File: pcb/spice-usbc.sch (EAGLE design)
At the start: 39 parts, among them J1 USB-C, J2 2X8, U1 MCP1700T-3302TT, U10 74LVC1G17, U11 74HC541, U12 74LVC1G17, U13 74LVC1G17, U14 74LVC1G17, U15 74LVC1G17, U16 74LVC1G17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

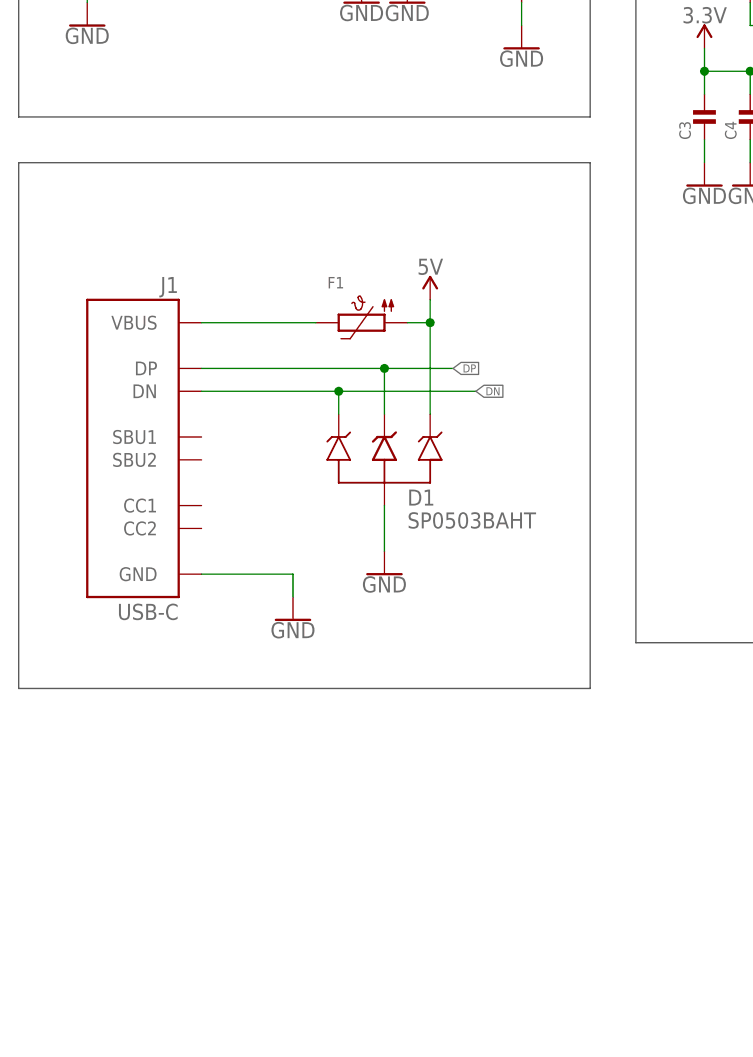
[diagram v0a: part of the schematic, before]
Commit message: Add USB C CC lines pull down
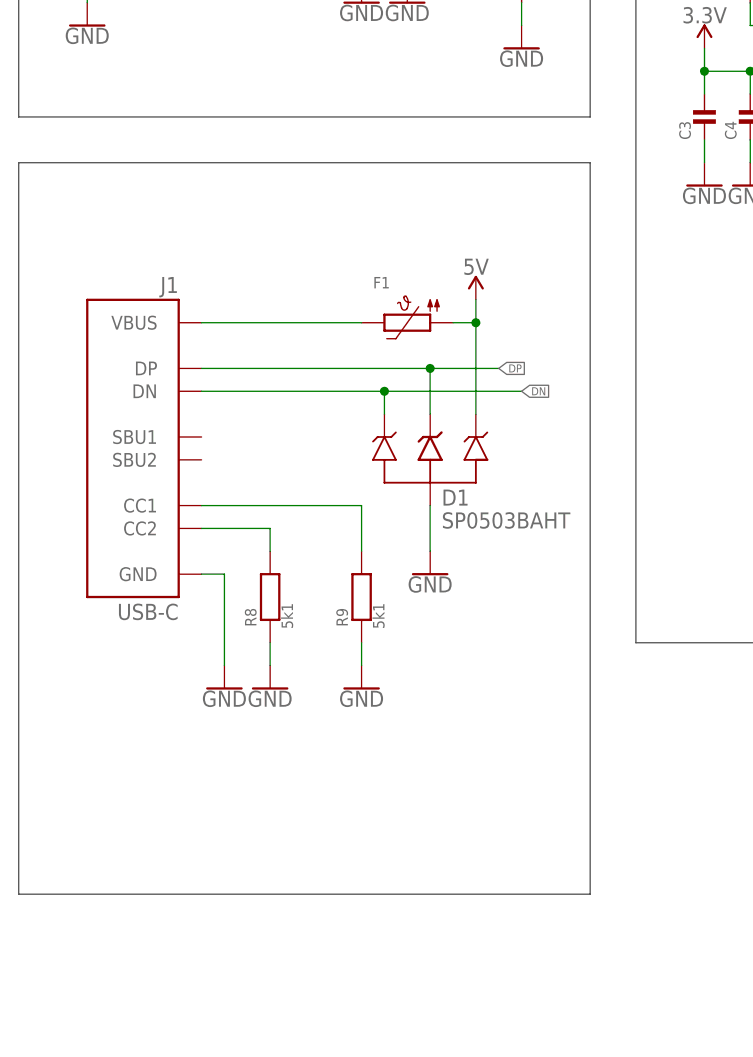
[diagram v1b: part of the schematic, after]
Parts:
- added R8, R9: 5k1, Passive Components > Resistors > Chip Resistors:RESISTOR0603
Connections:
- new net N$15: J1.CC2@B5, R8.P$2
- new net N$26: J1.CC1@A5, R9.P$2
- net GND: now also R8.P$1, R9.P$1
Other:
- moved on the sheet: D1, F1
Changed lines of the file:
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@@
 <?xml version="1.0" encoding="utf-8"?>
 <!DOCTYPE eagle SYSTEM "eagle.dtd">
-<eagle version="9.3.2">
+<eagle version="9.3.0">
 <drawing>
 <settings>
@@
 <part name="F1" library="Circuit Protection &gt; Resettable Fuses - PPTC" deviceset="PTC" device="1210"/>
 <part name="J1" library="Connectors &gt; USB" deviceset="USB-C" device=""/>
+<part name="R8" library="Passive Components &gt; Resistors &gt; Chip Resistors" deviceset="RESISTOR" device="0603" value="5k1"/>
+<part name="R9" library="Passive Components &gt; Resistors &gt; Chip Resistors" deviceset="RESISTOR" device="0603" value="5k1"/>
+<part name="GND31" library="Utility &gt; Power Symbols" deviceset="GND" device=""/>
+<part name="GND32" library="Utility &gt; Power Symbols" deviceset="GND" device=""/>
 </parts>
 <sheets>
@@
 <wire x1="10.16" y1="139.7" x2="10.16" y2="187.96" width="0.1524" layer="97"/>
 <wire x1="10.16" y1="134.62" x2="73.66" y2="134.62" width="0.1524" layer="97"/>
-<wire x1="73.66" y1="134.62" x2="73.66" y2="76.2" width="0.1524" layer="97"/>
-<wire x1="73.66" y1="76.2" x2="10.16" y2="76.2" width="0.1524" layer="97"/>
-<wire x1="10.16" y1="76.2" x2="10.16" y2="134.62" width="0.1524" layer="97"/>
+<wire x1="73.66" y1="134.62" x2="73.66" y2="53.34" width="0.1524" layer="97"/>
+<wire x1="73.66" y1="53.34" x2="10.16" y2="53.34" width="0.1524" layer="97"/>
+<wire x1="10.16" y1="53.34" x2="10.16" y2="134.62" width="0.1524" layer="97"/>
 <wire x1="172.72" y1="198.12" x2="284.48" y2="198.12" width="0.1524" layer="97"/>
 <wire x1="284.48" y1="198.12" x2="284.48" y2="63.5" width="0.1524" layer="97"/>
@@
 <attribute name="VALUE" x="68.58" y="161.544" size="1.27" layer="96" rot="R90"/>
 </instance>
-<instance part="D1" gate="G$1" x="50.8" y="99.06" smashed="yes">
-<attribute name="NAME" x="53.34" y="96.52" size="1.778" layer="95"/>
-<attribute name="VALUE" x="53.34" y="93.98" size="1.778" layer="95"/>
+<instance part="D1" gate="G$1" x="55.88" y="99.06" smashed="yes">
+<attribute name="NAME" x="57.15" y="96.52" size="1.778" layer="95"/>
+<attribute name="VALUE" x="57.15" y="93.98" size="1.778" layer="95"/>
 </instance>
 <instance part="C4" gate="G$1" x="91.44" y="139.7" smashed="yes">
@@
 <attribute name="VALUE" x="104.14" y="165.354" size="1.778" layer="96" align="bottom-center"/>
 </instance>
-<instance part="SUPPLY3" gate="G$1" x="55.88" y="119.38" smashed="yes">
-<attribute name="VALUE" x="55.88" y="122.174" size="1.778" layer="96" align="bottom-center"/>
+<instance part="SUPPLY3" gate="G$1" x="60.96" y="119.38" smashed="yes">
+<attribute name="VALUE" x="60.96" y="122.174" size="1.778" layer="96" align="bottom-center"/>
 </instance>
 <instance part="GND10" gate="1" x="104.14" y="116.84" smashed="yes">
@@
 <attribute name="VALUE" x="17.78" y="167.894" size="1.778" layer="96" align="bottom-center"/>
 </instance>
-<instance part="GND2" gate="1" x="40.64" y="83.82" smashed="yes">
-<attribute name="VALUE" x="40.64" y="83.566" size="1.778" layer="96" align="top-center"/>
-</instance>
-<instance part="GND4" gate="1" x="50.8" y="88.9" smashed="yes">
-<attribute name="VALUE" x="50.8" y="88.646" size="1.778" layer="96" align="top-center"/>
+<instance part="GND2" gate="1" x="33.02" y="76.2" smashed="yes">
+<attribute name="VALUE" x="33.02" y="75.946" size="1.778" layer="96" align="top-center"/>
+</instance>
+<instance part="GND4" gate="1" x="55.88" y="88.9" smashed="yes">
+<attribute name="VALUE" x="55.88" y="88.646" size="1.778" layer="96" align="top-center"/>
 </instance>
 <instance part="U9" gate=".1" x="200.66" y="119.38" smashed="yes">
@@
 <attribute name="VALUE" x="300.609" y="148.59" size="1.778" layer="96" rot="R90"/>
 </instance>
-<instance part="F1" gate="G$2" x="48.26" y="116.84" smashed="yes">
-<attribute name="NAME" x="44.45" y="120.65" size="1.27" layer="95"/>
-<attribute name="VALUE" x="44.45" y="113.03" size="1.27" layer="96"/>
+<instance part="F1" gate="G$2" x="53.34" y="116.84" smashed="yes">
+<attribute name="NAME" x="49.53" y="120.65" size="1.27" layer="95"/>
+<attribute name="VALUE" x="49.53" y="113.03" size="1.27" layer="96"/>
 </instance>
 <instance part="J1" gate="G$1" x="27.94" y="86.36" smashed="yes" rot="MR0">
 <attribute name="VALUE" x="27.94" y="83.82" size="1.778" layer="96" rot="MR0"/>
 <attribute name="NAME" x="27.94" y="121.92" size="1.778" layer="95" rot="MR0" align="top-left"/>
+</instance>
+<instance part="R8" gate="G$1" x="38.1" y="86.36" smashed="yes" rot="R90">
+<attribute name="NAME" x="36.576" y="83.058" size="1.27" layer="95" rot="R90"/>
+<attribute name="VALUE" x="40.64" y="82.804" size="1.27" layer="96" rot="R90"/>
+</instance>
+<instance part="R9" gate="G$1" x="48.26" y="86.36" smashed="yes" rot="R90">
+<attribute name="NAME" x="46.736" y="83.058" size="1.27" layer="95" rot="R90"/>
+<attribute name="VALUE" x="50.8" y="82.804" size="1.27" layer="96" rot="R90"/>
+</instance>
+<instance part="GND31" gate="1" x="38.1" y="76.2" smashed="yes">
+<attribute name="VALUE" x="38.1" y="75.946" size="1.778" layer="96" align="top-center"/>
+</instance>
+<instance part="GND32" gate="1" x="48.26" y="76.2" smashed="yes">
+<attribute name="VALUE" x="48.26" y="75.946" size="1.778" layer="96" align="top-center"/>
 </instance>
 </instances>
@@
 <segment>
 <pinref part="D1" gate="G$1" pin="2"/>
-<wire x1="45.72" y1="109.22" x2="45.72" y2="106.68" width="0.1524" layer="91"/>
-<wire x1="45.72" y1="109.22" x2="60.96" y2="109.22" width="0.1524" layer="91"/>
-<junction x="45.72" y="109.22"/>
-<label x="60.96" y="109.22" size="0.889" layer="95" xref="yes"/>
+<wire x1="50.8" y1="109.22" x2="50.8" y2="106.68" width="0.1524" layer="91"/>
+<wire x1="50.8" y1="109.22" x2="66.04" y2="109.22" width="0.1524" layer="91"/>
+<junction x="50.8" y="109.22"/>
+<label x="66.04" y="109.22" size="0.889" layer="95" xref="yes"/>
 <pinref part="J1" gate="G$1" pin="DN@A7,B7"/>
-<wire x1="45.72" y1="109.22" x2="30.48" y2="109.22" width="0.1524" layer="91"/>
+<wire x1="50.8" y1="109.22" x2="30.48" y2="109.22" width="0.1524" layer="91"/>
 </segment>
 </net>
@@
 <segment>
 <pinref part="D1" gate="G$1" pin="3"/>
-<wire x1="50.8" y1="111.76" x2="50.8" y2="106.68" width="0.1524" layer="91"/>
-<wire x1="50.8" y1="111.76" x2="58.42" y2="111.76" width="0.1524" layer="91"/>
-<junction x="50.8" y="111.76"/>
-<label x="58.42" y="111.76" size="0.889" layer="95" xref="yes"/>
+<wire x1="55.88" y1="111.76" x2="55.88" y2="106.68" width="0.1524" layer="91"/>
+<wire x1="55.88" y1="111.76" x2="63.5" y2="111.76" width="0.1524" layer="91"/>
+<junction x="55.88" y="111.76"/>
+<label x="63.5" y="111.76" size="0.889" layer="95" xref="yes"/>
 <pinref part="J1" gate="G$1" pin="DP@A6,B6"/>
-<wire x1="50.8" y1="111.76" x2="30.48" y2="111.76" width="0.1524" layer="91"/>
+<wire x1="55.88" y1="111.76" x2="30.48" y2="111.76" width="0.1524" layer="91"/>
 </segment>
 </net>
@@
 <pinref part="SUPPLY3" gate="G$1" pin="5V"/>
 <pinref part="D1" gate="G$1" pin="4"/>
-<wire x1="55.88" y1="119.38" x2="55.88" y2="116.84" width="0.1524" layer="91"/>
+<wire x1="60.96" y1="119.38" x2="60.96" y2="116.84" width="0.1524" layer="91"/>
 <pinref part="F1" gate="G$2" pin="1"/>
-<wire x1="55.88" y1="116.84" x2="55.88" y2="106.68" width="0.1524" layer="91"/>
-<wire x1="53.34" y1="116.84" x2="55.88" y2="116.84" width="0.1524" layer="91"/>
-<junction x="55.88" y="116.84"/>
+<wire x1="60.96" y1="116.84" x2="60.96" y2="106.68" width="0.1524" layer="91"/>
+<wire x1="58.42" y1="116.84" x2="60.96" y2="116.84" width="0.1524" layer="91"/>
+<junction x="60.96" y="116.84"/>
 </segment>
 <segment>
@@
 </segment>
 <segment>
-<wire x1="30.48" y1="88.9" x2="40.64" y2="88.9" width="0.1524" layer="91"/>
-<wire x1="40.64" y1="88.9" x2="40.64" y2="86.36" width="0.1524" layer="91"/>
+<wire x1="30.48" y1="88.9" x2="33.02" y2="88.9" width="0.1524" layer="91"/>
+<wire x1="33.02" y1="88.9" x2="33.02" y2="78.74" width="0.1524" layer="91"/>
 <pinref part="GND2" gate="1" pin="GND"/>
 <pinref part="J1" gate="G$1" pin="GND@A12,A1,B1,B12"/>
@@
 <segment>
 <pinref part="D1" gate="G$1" pin="1"/>
-<wire x1="50.8" y1="96.52" x2="50.8" y2="91.44" width="0.1524" layer="91"/>
+<wire x1="55.88" y1="96.52" x2="55.88" y2="91.44" width="0.1524" layer="91"/>
 <pinref part="GND4" gate="1" pin="GND"/>
 </segment>
@@
 <wire x1="297.18" y1="152.908" x2="297.18" y2="150.368" width="0.1524" layer="91"/>
 <pinref part="D5" gate="G$1" pin="P$2"/>
+</segment>
+<segment>
+<pinref part="GND32" gate="1" pin="GND"/>
+<pinref part="R9" gate="G$1" pin="P$1"/>
+<wire x1="48.26" y1="78.74" x2="48.26" y2="81.28" width="0.1524" layer="91"/>
+</segment>
+<segment>
+<pinref part="GND31" gate="1" pin="GND"/>
+<pinref part="R8" gate="G$1" pin="P$1"/>
+<wire x1="38.1" y1="78.74" x2="38.1" y2="81.28" width="0.1524" layer="91"/>
 </segment>
 </net>
@@
 <pinref part="F1" gate="G$2" pin="2"/>
 <pinref part="J1" gate="G$1" pin="VBUS@B9,B4,A4,A9"/>
-<wire x1="43.18" y1="116.84" x2="30.48" y2="116.84" width="0.1524" layer="91"/>
-</segment>
-</net>
+<wire x1="48.26" y1="116.84" x2="30.48" y2="116.84" width="0.1524" layer="91"/>
+</segment>
+</net>
+<net name="N$15" class="0">
+<segment>
+<pinref part="J1" gate="G$1" pin="CC2@B5"/>
+<pinref part="R8" gate="G$1" pin="P$2"/>
+<wire x1="30.48" y1="93.98" x2="38.1" y2="93.98" width="0.1524" layer="91"/>
+<wire x1="38.1" y1="93.98" x2="38.1" y2="91.44" width="0.1524" layer="91"/>
+</segment>
+</net>
+<net name="N$26" class="0">
+<segment>
+<pinref part="J1" gate="G$1" pin="CC1@A5"/>
+<pinref part="R9" gate="G$1" pin="P$2"/>
+<wire x1="30.48" y1="96.52" x2="48.26" y2="96.52" width="0.1524" layer="91"/>
+<wire x1="48.26" y1="96.52" x2="48.26" y2="91.44" width="0.1524" layer="91"/>
+</segment>
+</net>
